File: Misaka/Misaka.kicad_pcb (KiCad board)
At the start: 2 copper layers, 49 parts, among them J1 Conn_Coaxial_Power, J2 Conn_01x04_Male, J3 Conn_01x04_Male, J4 Conn_01x04_Male, SW1 SW_DIP_x03, U1 DRV8825PWPR, U2 ATmega2560-16AU, U3 DRV8825PWPR, U4 DRV8825PWPR

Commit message: CH340C
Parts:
- added C10: 100nF, Capacitor_SMD:C_0603_1608Metric, F.Cu at (43.5, 108.1)
- added C11: 100nF, Capacitor_SMD:C_0603_1608Metric, F.Cu at (61.4, 100.1)
- added C12: 100nF, Capacitor_SMD:C_0603_1608Metric, F.Cu at (61.4, 102.6)
- added C13: 22pF, Capacitor_SMD:C_0603_1608Metric, F.Cu at (61.4, 105.1)
- added D1: CD1206, Diode_SMD:D_1206_3216Metric_Pad1.42x1.75mm_HandSolder, F.Cu at (58.7, 97.1)
- added J5: USB_B_Micro, Connector_USB:USB_Micro-B_Wuerth_614105150721_Vertical, F.Cu at (49.4, 97.7)
- added R22: 1k, Resistor_SMD:R_0603_1608Metric_Pad1.05x0.95mm_HandSolder, F.Cu at (57.2, 106.6)
- added R23: 10k, Resistor_SMD:R_0603_1608Metric_Pad1.05x0.95mm_HandSolder, F.Cu at (57.2, 104.1)
- added R24: 1k, Resistor_SMD:R_0603_1608Metric_Pad1.05x0.95mm_HandSolder, F.Cu at (57.2, 101.6)
- added R25: 1k, Resistor_SMD:R_0603_1608Metric_Pad1.05x0.95mm_HandSolder, F.Cu at (39.4, 108.1)
- added S1: MOMENTARY-SWITCH-SPST-PTH-6.0MM, Switches:TACTILE_SWITCH_PTH_6.0MM, F.Cu at (50.3, 104.1)
- added U5: CH340C, Package_SO:SOIC-16_3.9x9.9mm_P1.27mm, F.Cu at (41.4, 101.1)
- moved C1 69.3 mm to (124.5, 62.2)
- moved R3 59.6 mm to (111.9, 68.3)
- moved R4 59.6 mm to (115.9, 64.7)
- moved R6 59.6 mm to (115.9, 62.2)
- moved C-VMA1 59.6 mm to (128.9, 59.7)
- moved C2 59.6 mm to (120.1, 64.7)
- moved CP1 59.6 mm to (129.0, 57.1)
- moved J2 59.6 mm to (116.3, 58.8)
- moved R1 59.6 mm to (124.7, 59.5)
- moved R2 59.6 mm to (120.3, 62.2)
- moved R5 59.6 mm to (124.7, 57.0)
- moved R7 59.6 mm to (107.6, 68.3)
- moved U1 59.6 mm to (109.6, 61.4)
- moved C-VMB1 56.1 mm to (116.1, 67.2)
- moved C3 53.5 mm to (120.1, 67.2)
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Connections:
- net /D18 renamed /TX1
- net /D19 renamed /RX1
- U2 pad 2: /D1 -> /RX0
- U2 pad 3: /D2 -> /TX0
- U2 pad 30: Net-(U2-Pad30) -> /RESET

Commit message: V1
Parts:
- added C14: 100nF, Capacitor_SMD:C_0603_1608Metric_Pad1.05x0.95mm_HandSolder, F.Cu at (59.7, 146.1)
- added C15: 1uF, Capacitor_SMD:C_0603_1608Metric_Pad1.05x0.95mm_HandSolder, F.Cu at (84.6, 140.3)
- added C16: 1uF, Capacitor_SMD:C_0603_1608Metric_Pad1.05x0.95mm_HandSolder, F.Cu at (88.9, 137.8)
- added C17: 100nF, Capacitor_SMD:C_0603_1608Metric_Pad1.05x0.95mm_HandSolder, F.Cu at (43.7, 129.0)
- added C18: 100nF, Capacitor_SMD:C_0603_1608Metric_Pad1.05x0.95mm_HandSolder, F.Cu at (39.4, 131.5)
- added C19: 100nF, Capacitor_SMD:C_0603_1608Metric_Pad1.05x0.95mm_HandSolder, F.Cu at (43.7, 131.5)
- added C20: 100nF, Capacitor_SMD:C_0603_1608Metric_Pad1.05x0.95mm_HandSolder, F.Cu at (48.1, 129.0)
- added C21: 100nF, Capacitor_SMD:C_0603_1608Metric_Pad1.05x0.95mm_HandSolder, F.Cu at (52.4, 129.0)
- added C22: 100nF, Capacitor_SMD:C_0603_1608Metric_Pad1.05x0.95mm_HandSolder, F.Cu at (39.4, 129.0)
- added C23: 100nF, Capacitor_SMD:C_0603_1608Metric_Pad1.05x0.95mm_HandSolder, F.Cu at (48.1, 131.5)
- added C24: 100nF, Capacitor_SMD:C_0603_1608Metric_Pad1.05x0.95mm_HandSolder, F.Cu at (52.4, 131.5)
- added CP4: 47uF, Capacitor_SMD:CP_Elec_6.3x5.8, F.Cu at (42.4, 148.8)
- added CP5: 47uF, Capacitor_SMD:CP_Elec_6.3x5.8, F.Cu at (42.4, 140.6)
- added D10: WS2812B, LED_SMD:LED_WS2812B_PLCC4_5.0x5.0mm_P3.2mm, F.Cu at (66.7, 117.8)
- added D2: M7, Diode_SMD:D_SMA_Handsoldering, F.Cu at (52.7, 138.8)
- added D3: WS2812B, LED_SMD:LED_WS2812B_PLCC4_5.0x5.0mm_P3.2mm, F.Cu at (41.4, 124.4)
- added D4: WS2812B, LED_SMD:LED_WS2812B_PLCC4_5.0x5.0mm_P3.2mm, F.Cu at (49.8, 117.8)
- added D5: WS2812B, LED_SMD:LED_WS2812B_PLCC4_5.0x5.0mm_P3.2mm, F.Cu at (49.8, 124.4)
- added D6: WS2812B, LED_SMD:LED_WS2812B_PLCC4_5.0x5.0mm_P3.2mm, F.Cu at (58.3, 117.8)
- added D7: WS2812B, LED_SMD:LED_WS2812B_PLCC4_5.0x5.0mm_P3.2mm, F.Cu at (58.3, 124.4)
- added D8: WS2812B, LED_SMD:LED_WS2812B_PLCC4_5.0x5.0mm_P3.2mm, F.Cu at (41.4, 117.8)
- added D9: WS2812B, LED_SMD:LED_WS2812B_PLCC4_5.0x5.0mm_P3.2mm, F.Cu at (66.7, 124.4)
- added ICSP1: Conn_02x03_Odd_Even, Connector_PinHeader_2.54mm:PinHeader_2x03_P2.54mm_Vertical, F.Cu at (103.0, 116.8)
- added J6: Conn_01x04_Female, Connector_PinHeader_2.54mm:PinHeader_1x04_P2.54mm_Vertical, F.Cu at (127.0, 142.2)
- added J7: Conn_01x04_Female_UART, Connector_PinSocket_2.54mm:PinSocket_1x04_P2.54mm_Vertical, F.Cu at (76.4, 116.8)
- added J8: Conn_02x04_Odd_Even, Connector_PinSocket_1.27mm:PinSocket_2x04_P1.27mm_Vertical, F.Cu at (76.2, 138.2)
- added J9: Conn_01x07, Connector_PinSocket_2.54mm:PinSocket_1x07_P2.54mm_Vertical, F.Cu at (127.0, 119.0)
- added L1: LED, LED_SMD:LED_0603_1608Metric_Pad1.05x0.95mm_HandSolder, F.Cu at (75.2, 151.4)
- added LED1: ON, LED_SMD:LED_0603_1608Metric_Pad1.05x0.95mm_HandSolder, F.Cu at (49.9, 150.6)
- added R26: 1M, Resistor_SMD:R_0603_1608Metric_Pad1.05x0.95mm_HandSolder, F.Cu at (110.1, 120.8)
- added R27: 1k, Resistor_SMD:R_0603_1608Metric_Pad1.05x0.95mm_HandSolder, F.Cu at (54.2, 150.6)
- added R28: 1k, Resistor_SMD:R_0603_1608Metric_Pad1.05x0.95mm_HandSolder, F.Cu at (75.1, 144.9)
- added R29: 4.7k, Resistor_SMD:R_0603_1608Metric_Pad1.05x0.95mm_HandSolder, F.Cu at (80.2, 137.8)
- added R30: 4.7k, Resistor_SMD:R_0603_1608Metric_Pad1.05x0.95mm_HandSolder, F.Cu at (84.6, 137.8)
- added R31: 4.7k, Resistor_SMD:R_0603_1608Metric_Pad1.05x0.95mm_HandSolder, F.Cu at (80.2, 140.3)
- added R32: 4.7k, Resistor_SMD:R_0603_1608Metric_Pad1.05x0.95mm_HandSolder, F.Cu at (79.5, 144.9)
- added R33: 1k, Resistor_SMD:R_0603_1608Metric_Pad1.05x0.95mm_HandSolder, F.Cu at (79.5, 154.0)
- added R34: 1k, Resistor_SMD:R_0603_1608Metric_Pad1.05x0.95mm_HandSolder, F.Cu at (83.9, 151.4)
- added R35: 1k, Resistor_SMD:R_0603_1608Metric_Pad1.05x0.95mm_HandSolder, F.Cu at (83.9, 154.0)
- added RX1: LED, LED_SMD:LED_0603_1608Metric_Pad1.05x0.95mm_HandSolder, F.Cu at (75.2, 154.0)
- added TX1: LED, LED_SMD:LED_0603_1608Metric_Pad1.05x0.95mm_HandSolder, F.Cu at (79.6, 151.4)
- added U6: AMS1117-5.0, Package_TO_SOT_SMD:SOT-223-3_TabPin2, F.Cu at (52.6, 145.2)
- added U7: AMS1117-3.3, Package_TO_SOT_SMD:SOT-223-3_TabPin2, F.Cu at (62.6, 140.7)
- added U8: 24LC02, Package_DIP:DIP-8_W7.62mm_Socket_LongPads, F.Cu at (131.3, 118.8)
- added Y1: CSTLS16M0X51-B0, Crystal:Resonator_muRata_CSTLSxxxX-3Pin_W5.5mm_H3.0mm, F.Cu at (109.5, 117.0)
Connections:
- net Net-(U2-Pad63) renamed /RX3
- net Net-(U2-Pad64) renamed /TX3
- MOD1 pad 3: /TX1 -> Net-(MOD1-Pad3)
- R24 pad 1: /RX0 -> /TX0
- R25 pad 1: /TX0 -> /RX0
- U2 pad 100: Net-(U2-Pad100) -> +5V
- U2 pad 12: Net-(U2-Pad12) -> /RX2
- U2 pad 13: Net-(U2-Pad13) -> /TX2
- U2 pad 20: /D52 -> /SCK
- U2 pad 21: /D51 -> /MOSI
- U2 pad 22: /D50 -> /MISO
- U2 pad 43: Net-(U2-Pad43) -> /SCL
- U2 pad 44: Net-(U2-Pad44) -> /SDA
- U2 pad 7: Net-(U2-Pad7) -> /D3

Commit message: route v1.0
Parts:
- J8: moved to B.Cu
- moved RX1 125.2 mm to (110.5, 34.0)
- moved L1 124.0 mm to (114.9, 34.0)
- moved R33 124.0 mm to (119.2, 36.5)
- moved R34 122.7 mm to (119.3, 33.9)
- moved R35 121.5 mm to (114.9, 36.5)
- moved TX1 119.0 mm to (110.5, 36.6)
- moved U6 113.8 mm to (119.0, 52.8)
- moved R27 111.2 mm to (116.1, 58.1)
- moved CP4 104.4 mm to (98.8, 60.9)
- moved CP5 104.4 mm to (98.8, 52.7)
- moved D2 104.4 mm to (109.1, 50.9)
- moved LED1 104.4 mm to (106.3, 62.7)
- moved C14 97.7 mm to (110.6, 62.7)
- moved D3 96.1 mm to (83.3, 38.0)
- moved U7 95.4 mm to (109.0, 57.3)
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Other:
- board outline added: 100 x 100 mm

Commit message: route v1.1
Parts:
- J2, J3, J4: moved to B.Cu
- moved R33 107.5 mm to (34.5, 102.8)
- moved R34 106.4 mm to (34.5, 98.2)
- moved TX1 104.3 mm to (30.0, 102.8)
- moved L1 103.5 mm to (30.0, 93.2)
- moved RX1 103.0 mm to (30.0, 98.2)
- moved R35 98.4 mm to (34.5, 93.2)
- moved R27 95.4 mm to (34.6, 107.8)
- moved J6 91.2 mm to (30.0, 83.5), turned to 180 degrees
- moved LED1 88.4 mm to (30.1, 107.8)
- moved D10 85.8 mm to (115.2, 102.0)
- moved C24 82.4 mm to (121.8, 102.0), turned to 270 degrees
- moved D9 79.4 mm to (115.2, 94.0)
- moved C22 78.8 mm to (121.8, 86.0), turned to 270 degrees
- moved C23 78.5 mm to (121.8, 94.0), turned to 270 degrees
- moved C11 76.4 mm to (63.5, 27.2)
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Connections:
- MOD1 pad 3: Net-(MOD1-Pad3) -> /TX1
- U1 pad 10: Net-(J2-Pad2) -> Net-(J2-Pad1)
- U1 pad 8: Net-(J2-Pad1) -> Net-(J2-Pad2)
- U3 pad 10: Net-(J3-Pad2) -> Net-(J3-Pad1)
- U3 pad 8: Net-(J3-Pad1) -> Net-(J3-Pad2)
- U4 pad 10: Net-(J4-Pad2) -> Net-(J4-Pad1)
- U4 pad 8: Net-(J4-Pad1) -> Net-(J4-Pad2)
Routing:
- net +5V: track 0.00 -> 357.3 mm, vias 0 -> 3
- net GND: track 0.00 -> 250.3 mm
- net +3V3: track 0.00 -> 179.3 mm, vias 0 -> 2
- net +12V: track 0.00 -> 158.8 mm
- net /RESET: track 0.00 -> 104.9 mm, vias 0 -> 3
- net /RX0: track 0.00 -> 63.5 mm, vias 0 -> 2
- net /TX0: track 0.00 -> 60.4 mm, vias 0 -> 2
- net /MS3: track 0.00 -> 59.8 mm
- net /TX1: track 0.00 -> 59.0 mm, vias 0 -> 2
- net /RX1: track 0.00 -> 57.1 mm
- net /SCL: track 0.00 -> 47.0 mm
- net /CameraModule/E2PROM-SDA: track 0.00 -> 39.1 mm
- net Net-(C14-Pad1): track 0.00 -> 38.1 mm
- net /CameraModule/EFUSE: track 0.00 -> 30.5 mm
- net /CameraModule/E2PROM-SCK: track 0.00 -> 28.8 mm
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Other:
- outline, holes or cut-outs redrawn

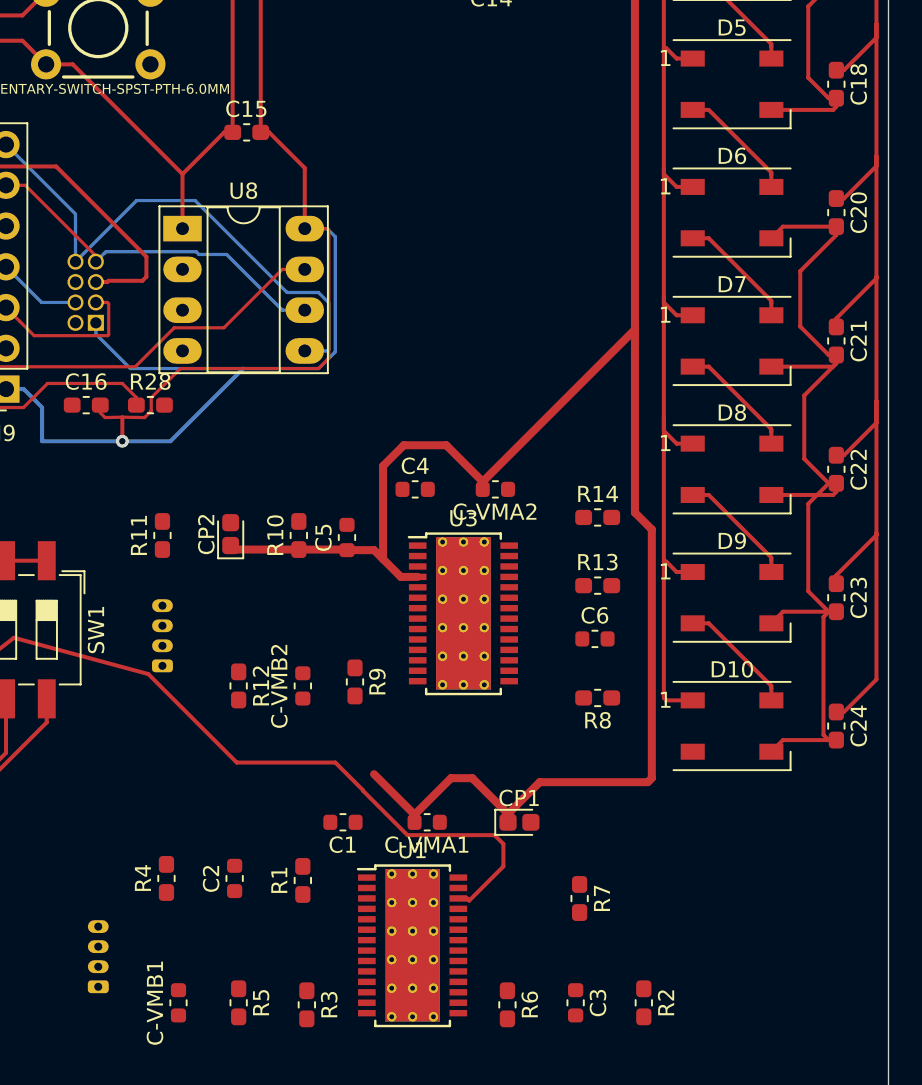
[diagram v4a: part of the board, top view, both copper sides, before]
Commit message: Begin Free Routing
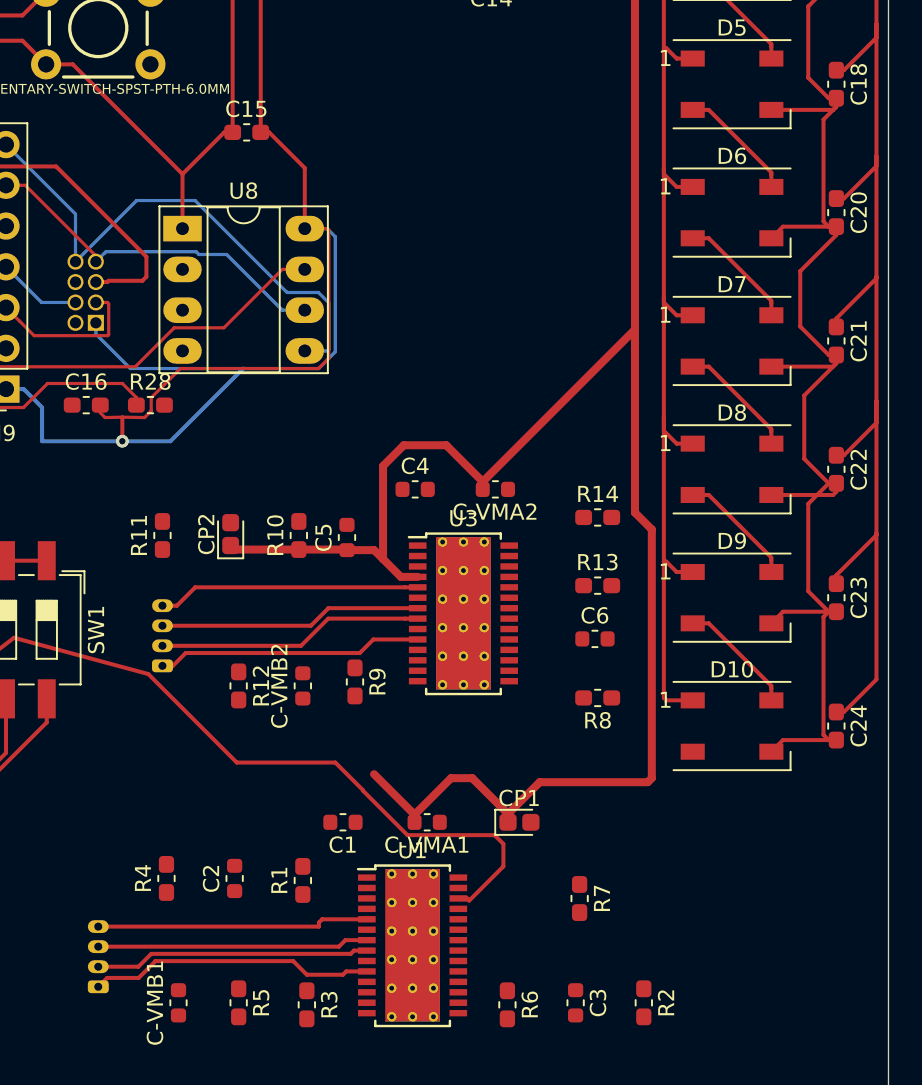
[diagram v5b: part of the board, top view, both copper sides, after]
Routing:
- net Net-(J2-Pad1): track 0.00 -> 17.8 mm
- net Net-(J2-Pad2): track 0.00 -> 17.2 mm
- net Net-(J2-Pad4): track 0.00 -> 17.1 mm
- net Net-(J2-Pad3): track 0.00 -> 16.9 mm
- net Net-(J3-Pad2): track 0.00 -> 16.6 mm
- net Net-(J3-Pad1): track 0.00 -> 16.6 mm
- net Net-(J3-Pad4): track 0.00 -> 16.4 mm
- net Net-(J3-Pad3): track 0.00 -> 16.4 mm
- net GND: track 250.3 -> 258.7 mm
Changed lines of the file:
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@@
     (thickness 1.6)
     (drawings 5)
-    (tracks 745)
+    (tracks 785)
     (zones 0)
     (modules 106)
@@
   (segment (start 121.55 55.6) (end 121.75 55.4) (width 0.25) (layer F.Cu) (net 6))
   (segment (start 117.7 55.6) (end 121.55 55.6) (width 0.25) (layer F.Cu) (net 6))
-  (segment (start 121.75 63.4) (end 121.75 62.875) (width 0.25) (layer F.Cu) (net 6))
   (segment (start 121.55 63.6) (end 121.75 63.4) (width 0.25) (layer F.Cu) (net 6))
   (segment (start 117.7 63.6) (end 121.55 63.6) (width 0.25) (layer F.Cu) (net 6))
@@
   (segment (start 120.94999 102.54999) (end 120.94999 95.20001) (width 0.25) (layer F.Cu) (net 6))
   (segment (start 121.75 102.875) (end 121.275 102.875) (width 0.25) (layer F.Cu) (net 6))
+  (segment (start 121.275 70.875) (end 121.75 70.875) (width 0.25) (layer F.Cu) (net 6))
+  (segment (start 120.94999 70.54999) (end 121.275 70.875) (width 0.25) (layer F.Cu) (net 6))
+  (segment (start 120.94999 64.20001) (end 120.94999 70.54999) (width 0.25) (layer F.Cu) (net 6))
+  (segment (start 121.75 63.4) (end 120.94999 64.20001) (width 0.25) (layer F.Cu) (net 6))
+  (segment (start 121.75 62.875) (end 121.75 63.4) (width 0.25) (layer F.Cu) (net 6))
   (segment (start 54.1 109.675) (end 54.9 109.675) (width 0.25) (layer F.Cu) (net 11))
   (segment (start 54.024999 105.693507) (end 54.024999 109.599999) (width 0.25) (layer F.Cu) (net 11))
@@
   (segment (start 58.875 121.525) (end 60.6 119.8) (width 0.25) (layer F.Cu) (net 14))
   (segment (start 58.875 122) (end 58.875 121.525) (width 0.25) (layer F.Cu) (net 14))
+  (segment (start 75.75 114.5) (end 89.5 114.5) (width 0.25) (layer F.Cu) (net 15))
+  (segment (start 89.5 114.5) (end 89.5 114.25) (width 0.25) (layer F.Cu) (net 15))
+  (segment (start 89.705 114.045) (end 92.49 114.045) (width 0.25) (layer F.Cu) (net 15))
+  (segment (start 89.5 114.25) (end 89.705 114.045) (width 0.25) (layer F.Cu) (net 15))
+  (segment (start 75.75 115.75) (end 90.75 115.75) (width 0.25) (layer F.Cu) (net 16))
+  (segment (start 91.155 115.345) (end 92.49 115.345) (width 0.25) (layer F.Cu) (net 16))
+  (segment (start 90.75 115.75) (end 91.155 115.345) (width 0.25) (layer F.Cu) (net 16))
+  (segment (start 75.75 117) (end 78.25 117) (width 0.25) (layer F.Cu) (net 17))
+  (segment (start 91.69 115.995) (end 92.49 115.995) (width 0.25) (layer F.Cu) (net 17))
+  (segment (start 91.48499 116.20001) (end 91.69 115.995) (width 0.25) (layer F.Cu) (net 17))
+  (segment (start 79.04999 116.20001) (end 91.48499 116.20001) (width 0.25) (layer F.Cu) (net 17))
+  (segment (start 78.25 117) (end 79.04999 116.20001) (width 0.25) (layer F.Cu) (net 17))
+  (segment (start 76.30001 117.69999) (end 78.268235 117.69999) (width 0.25) (layer F.Cu) (net 18))
+  (segment (start 75.75 118.25) (end 76.30001 117.69999) (width 0.25) (layer F.Cu) (net 18))
+  (segment (start 78.268235 117.69999) (end 79.318205 116.65002) (width 0.25) (layer F.Cu) (net 18))
+  (segment (start 79.318205 116.65002) (end 87.90002 116.65002) (width 0.25) (layer F.Cu) (net 18))
+  (segment (start 87.90002 116.65002) (end 88.75 117.5) (width 0.25) (layer F.Cu) (net 18))
+  (segment (start 88.75 117.5) (end 91 117.5) (width 0.25) (layer F.Cu) (net 18))
+  (segment (start 91.205 117.295) (end 92.49 117.295) (width 0.25) (layer F.Cu) (net 18))
+  (segment (start 91 117.5) (end 91.205 117.295) (width 0.25) (layer F.Cu) (net 18))
+  (segment (start 94.86 93.355) (end 95.66 93.355) (width 0.25) (layer F.Cu) (net 19))
+  (segment (start 81.795 93.355) (end 94.86 93.355) (width 0.25) (layer F.Cu) (net 19))
+  (segment (start 80.65 94.5) (end 81.795 93.355) (width 0.25) (layer F.Cu) (net 19))
+  (segment (start 79.75 94.5) (end 80.65 94.5) (width 0.25) (layer F.Cu) (net 19))
+  (segment (start 79.75 95.75) (end 89 95.75) (width 0.25) (layer F.Cu) (net 20))
+  (segment (start 90.095 94.655) (end 95.66 94.655) (width 0.25) (layer F.Cu) (net 20))
+  (segment (start 89 95.75) (end 90.095 94.655) (width 0.25) (layer F.Cu) (net 20))
+  (segment (start 94.86 95.305) (end 95.66 95.305) (width 0.25) (layer F.Cu) (net 21))
+  (segment (start 90.08141 95.305) (end 94.86 95.305) (width 0.25) (layer F.Cu) (net 21))
+  (segment (start 88.38641 97) (end 90.08141 95.305) (width 0.25) (layer F.Cu) (net 21))
+  (segment (start 79.75 97) (end 88.38641 97) (width 0.25) (layer F.Cu) (net 21))
+  (segment (start 81.19999 97.45001) (end 92.04999 97.45001) (width 0.25) (layer F.Cu) (net 22))
+  (segment (start 79.75 98.25) (end 80.4 98.25) (width 0.25) (layer F.Cu) (net 22))
+  (segment (start 80.4 98.25) (end 81.19999 97.45001) (width 0.25) (layer F.Cu) (net 22))
+  (segment (start 92.895 96.605) (end 95.66 96.605) (width 0.25) (layer F.Cu) (net 22))
+  (segment (start 92.04999 97.45001) (end 92.895 96.605) (width 0.25) (layer F.Cu) (net 22))
   (segment (start 54.1 111.625) (end 54.9 111.625) (width 0.25) (layer F.Cu) (net 23))
   (segment (start 42.15 111) (end 42.775 111.625) (width 0.25) (layer F.Cu) (net 23))
